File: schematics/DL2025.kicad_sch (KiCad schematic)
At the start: 8 parts, among them J1 Micro_SD_Card, U1 ATmega328PB-A, U2 DS18B20, U3 BMP280, U6 AMS1117-3.3, U7 AMS1117-3.3, U8 CC56-12GWA, U9 AMS1117-3.3

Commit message: Add files via upload
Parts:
- added U4: SC16IS750xPW, Package_SO:TSSOP-24_4.4x7.8mm_P0.65mm, symbol Interface_UART:SC16IS750xPW
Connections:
- net +5V: now also U4.7 (VDD)
- net GND: now also U3.1 (GND), U4.19 (VSS); no longer J1.5 (CLK), U1.17 (PB5)
- net at J1.3 (CMD), U1.16 (PB4): no longer J1.4 (VDD), U9.2 (VO)
- net at U1.30 (PD0): now also U4.2 (TX)
- net at U1.31 (PD1): now also U4.3 (RX)
- net at U3.2 (CSB): now also U3.6 (VDDIO), U3.8 (VDD), U6.2 (VO); no longer U3.1 (GND)
- net at U3.5 (SDO): no longer U3.6 (VDDIO)
- new net: J1.5 (CLK), U1.17 (PB5)
- new net: J1.4 (VDD), U9.2 (VO)
- no-connect marks 0 -> 34
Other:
- note added: "SDO POWINNO BYĆ PODŁĄCZONE DO GND LUB VCC ALE NIE DZIAŁA XD"
- moved on the sheet: U3

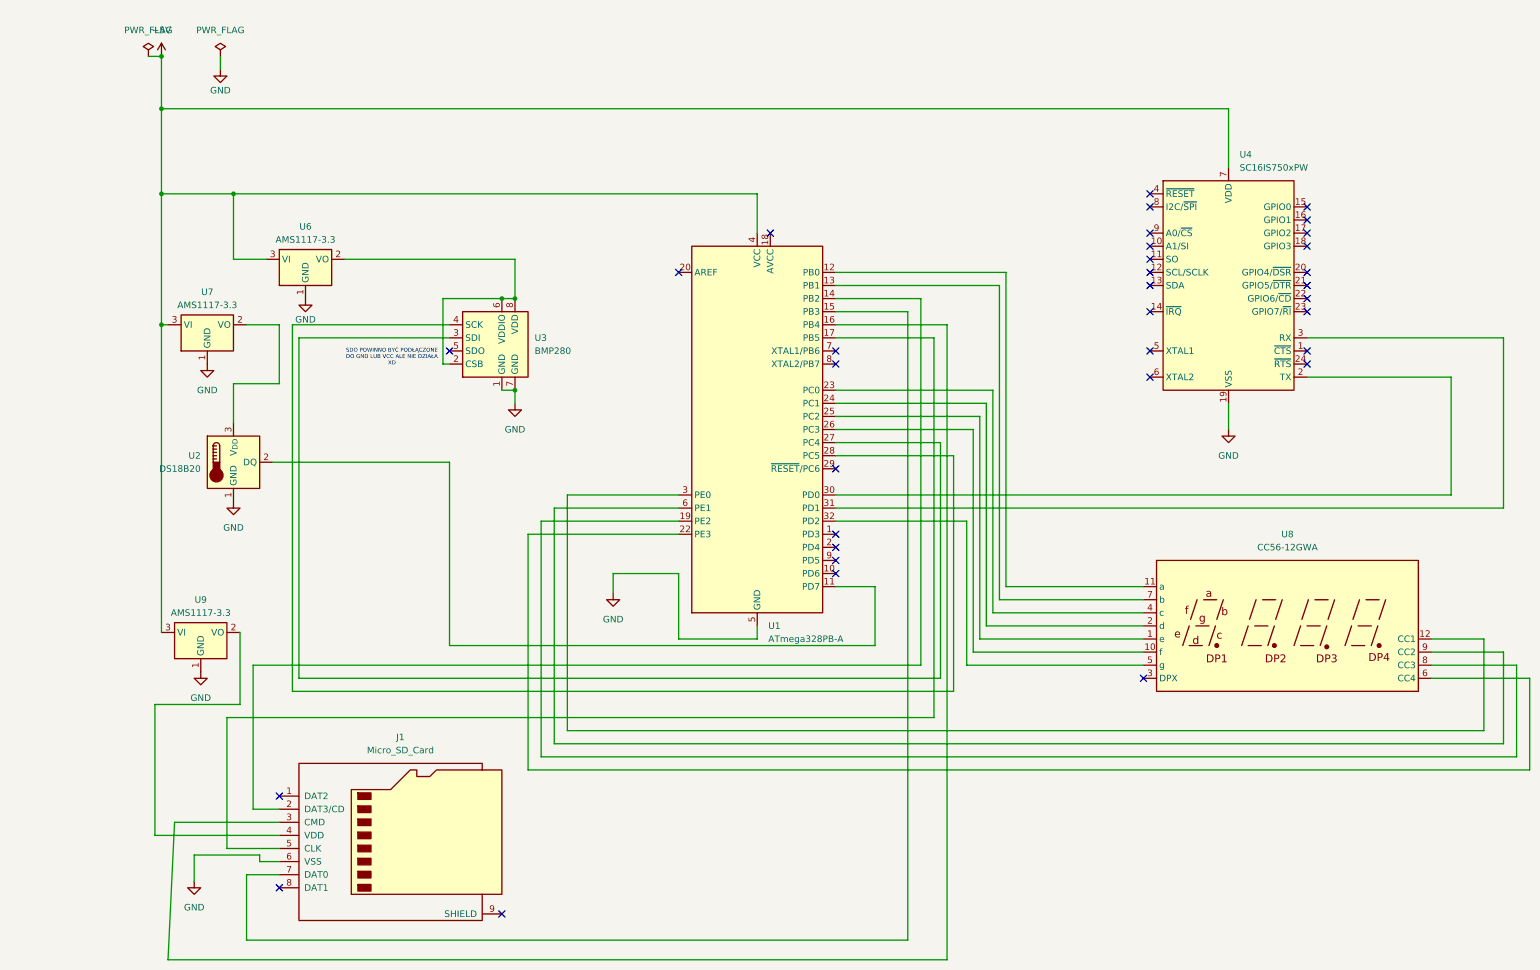
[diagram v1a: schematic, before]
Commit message: Updated schematics, just one AMS1117
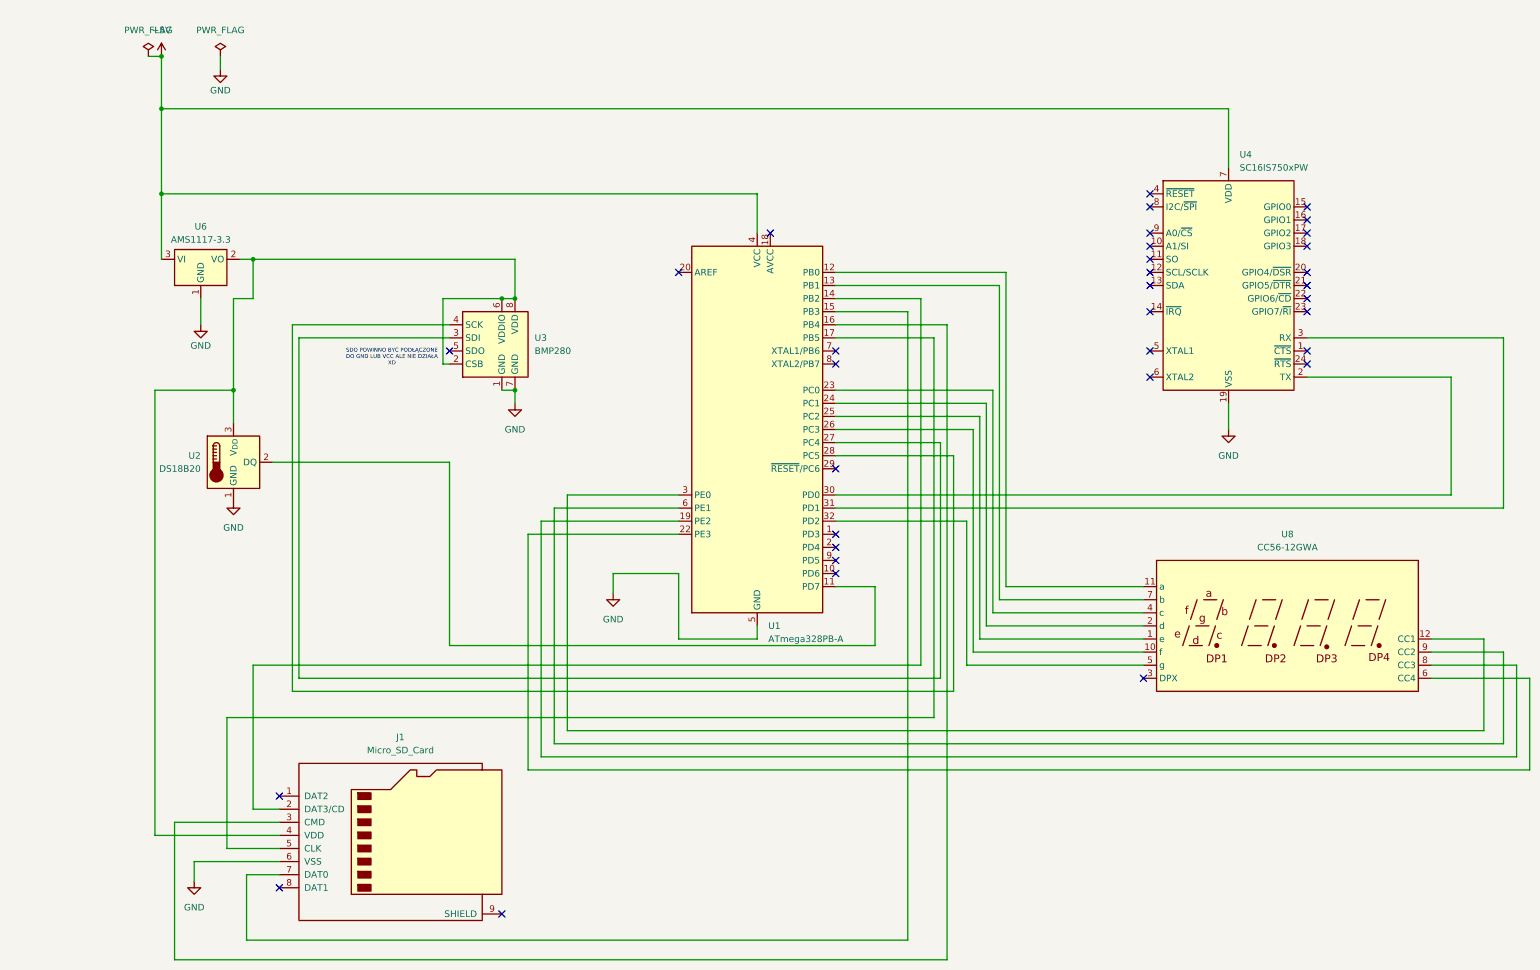
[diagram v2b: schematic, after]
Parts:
- removed U7, U9: AMS1117-3.3, Package_TO_SOT_SMD:SOT-223-3_TabPin2, symbol Regulator_Linear:AMS1117-3.3
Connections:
- net at J1.4 (VDD): now also U2.3 (V_{DD}), U3.2 (CSB), U3.6 (VDDIO), U3.8 (VDD), U6.2 (VO)
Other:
- moved on the sheet: U6

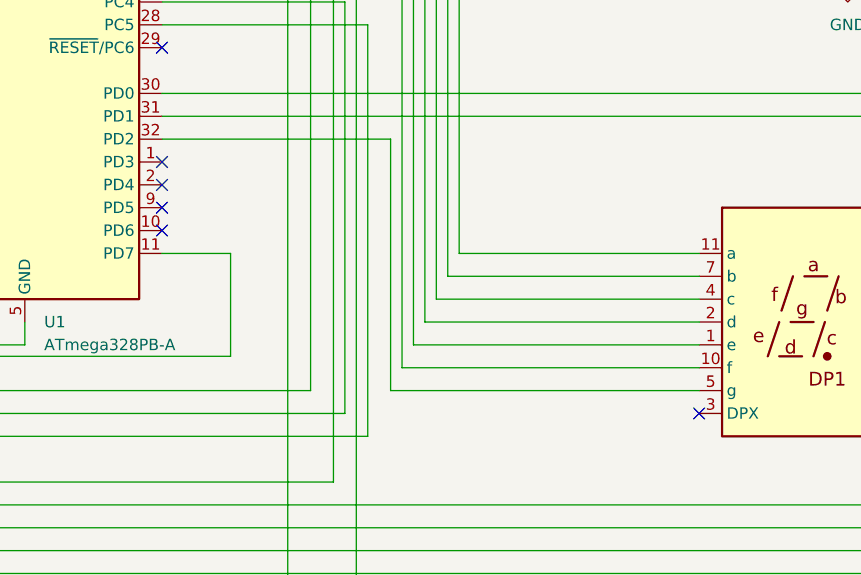
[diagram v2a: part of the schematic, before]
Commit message: Updated schematics, added LCD_DP -> PC3 connection
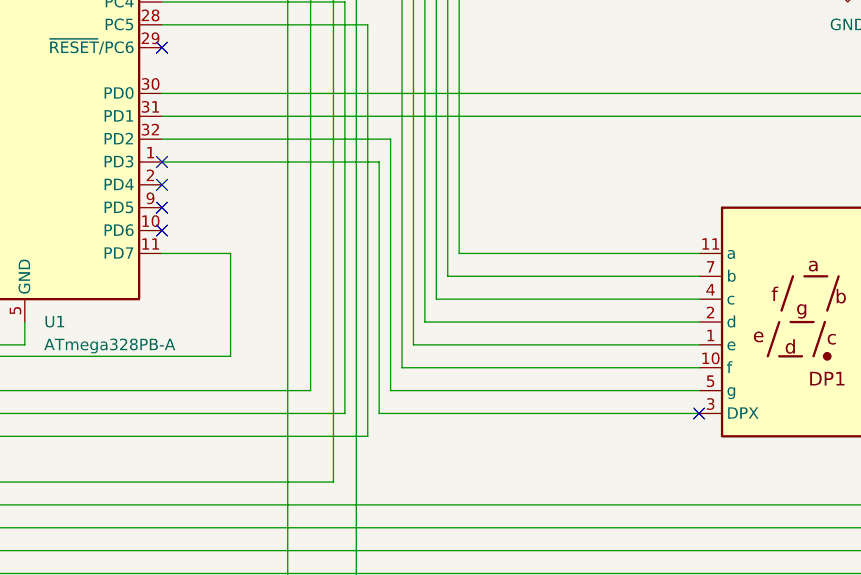
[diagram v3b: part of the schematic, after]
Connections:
- net at U1.1 (PD3): now also U8.3 (DPX)
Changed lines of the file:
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@@
+	(wire
+		(pts
+			(xy 148.59 111.76) (xy 172.72 111.76)
+		)
+		(stroke
+			(width 0)
+			(type default)
+		)
+	)
 	(wire
 		(pts
@@
 	(wire
 		(pts
+			(xy 172.72 139.7) (xy 208.28 139.7)
+		)
+		(stroke
+			(width 0)
+			(type default)
+		)
+	)
+	(wire
+		(pts
 			(xy 17.78 19.05) (xy 17.78 29.21)
 		)
@@
 		)
 		(stroke
+			(width 0)
+			(type default)
+		)
+	)
+	(wire
+		(pts
+			(xy 172.72 111.76) (xy 172.72 139.7)
+		)
+		(stroke

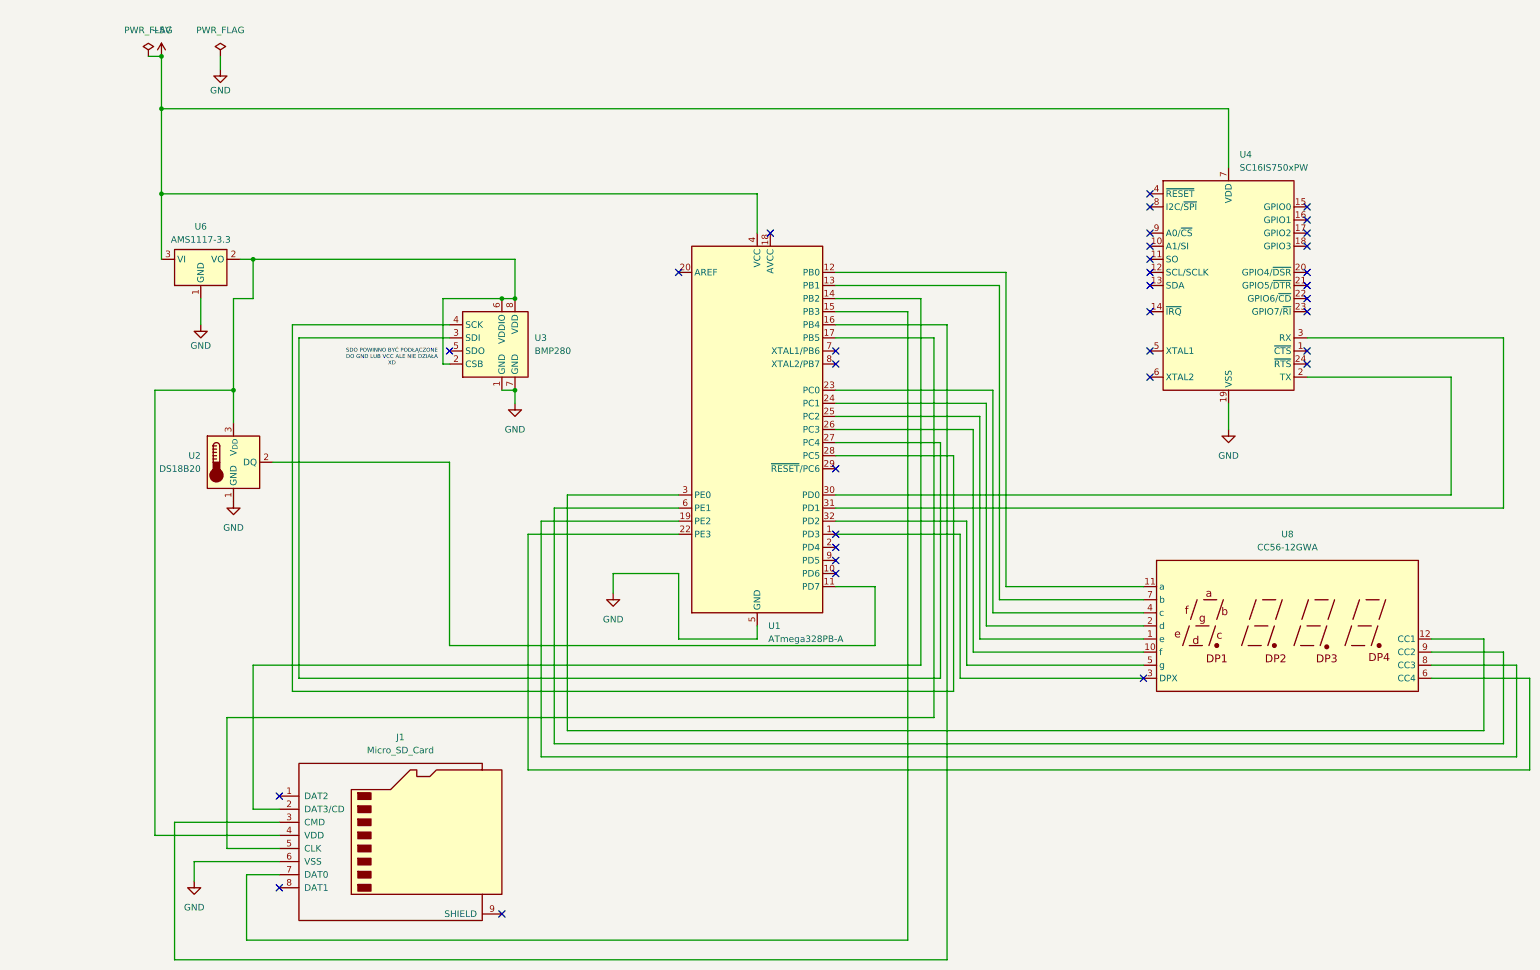
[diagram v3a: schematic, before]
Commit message: updated schematic, added capacitors
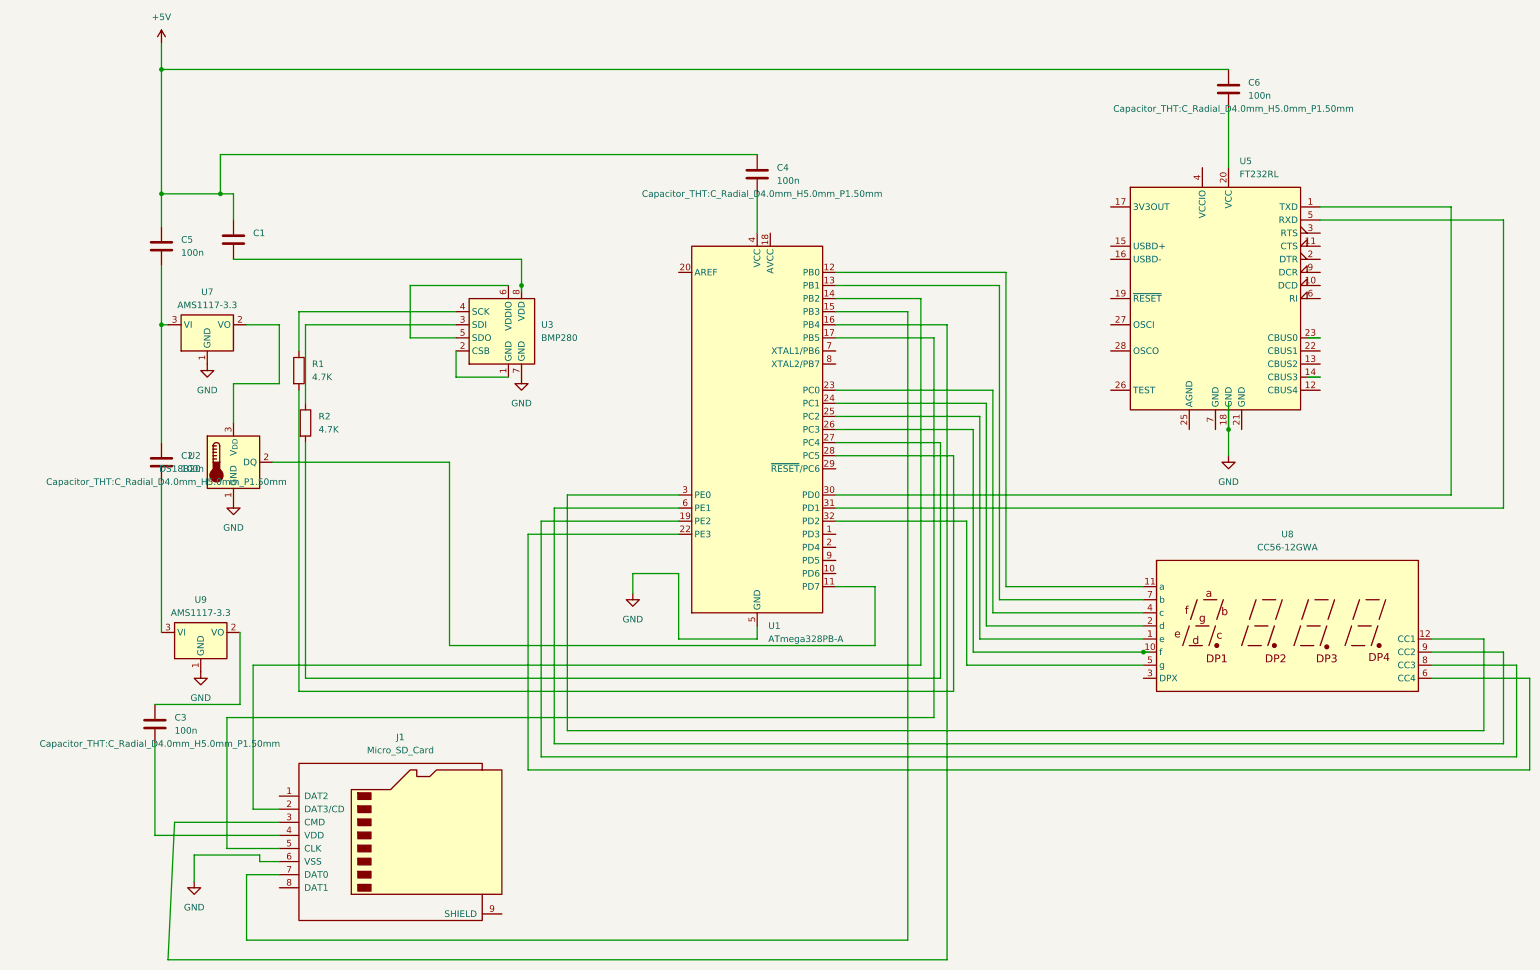
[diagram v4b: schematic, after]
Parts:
- removed U4: SC16IS750xPW, Package_SO:TSSOP-24_4.4x7.8mm_P0.65mm, symbol Interface_UART:SC16IS750xPW
- removed U6: AMS1117-3.3, Package_TO_SOT_SMD:SOT-223-3_TabPin2, symbol Regulator_Linear:AMS1117-3.3
- added C1, C2, C3, C4, C5, C6: 100n, Capacitor_THT:C_Radial_D4.0mm_H5.0mm_P1.50mm, symbol Device:C
- added R1, R2: 4.7K, Resistor_THT:R_Axial_DIN0207_L6.3mm_D2.5mm_P2.54mm_Vertical, symbol Device:R
- added U5: FT232RL, Package_SO:SSOP-28_5.3x10.2mm_P0.65mm, symbol Interface_USB:FT232RL
- added U7, U9: AMS1117-3.3, Package_TO_SOT_SMD:SOT-223-3_TabPin2, symbol Regulator_Linear:AMS1117-3.3
- J1: footprint (none) -> Connector_PinHeader_1.00mm:PinHeader_1x09_P1.00mm_Horizontal
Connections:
- net +5V: now also C1.1, C4.1, C5.1, C6.1; no longer U1.4 (VCC)
- net GND: now also U5.18 (GND), U7.1 (GND), U9.1 (GND); no longer U3.1 (GND)
- net at U1.1 (PD3): no longer U8.3 (DPX)
- net at U1.27 (PC4): now also R2.2; no longer U3.3 (SDI)
- net at U1.28 (PC5): now also R1.2; no longer U3.4 (SCK)
- net at U1.30 (PD0): now also U5.1 (TXD)
- net at U1.31 (PD1): now also U5.5 (RXD)
- net at U3.5 (SDO): now also U3.6 (VDDIO)
- new net: C3.1, U9.2 (VO)
- new net: C3.2, J1.4 (VDD)
- new net: C4.2, U1.4 (VCC)
- new net: C2.1, C5.2, U7.3 (VI)
- new net: C6.2, U5.20 (VCC)
- new net: C2.2, U9.3 (VI)
- new net: U3.1 (GND), U3.2 (CSB)
- new net: R2.1, U3.3 (SDI)
- new net: R1.1, U3.4 (SCK)
- new net: C1.2, U3.8 (VDD)
- new net: U2.3 (V_{DD}), U7.2 (VO)
- no-connect marks 34 -> 0
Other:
- note removed: "SDO POWINNO BYĆ PODŁĄCZONE DO GND LUB VCC ALE NIE DZIAŁA XD"
- moved on the sheet: U3

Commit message: updated schematics
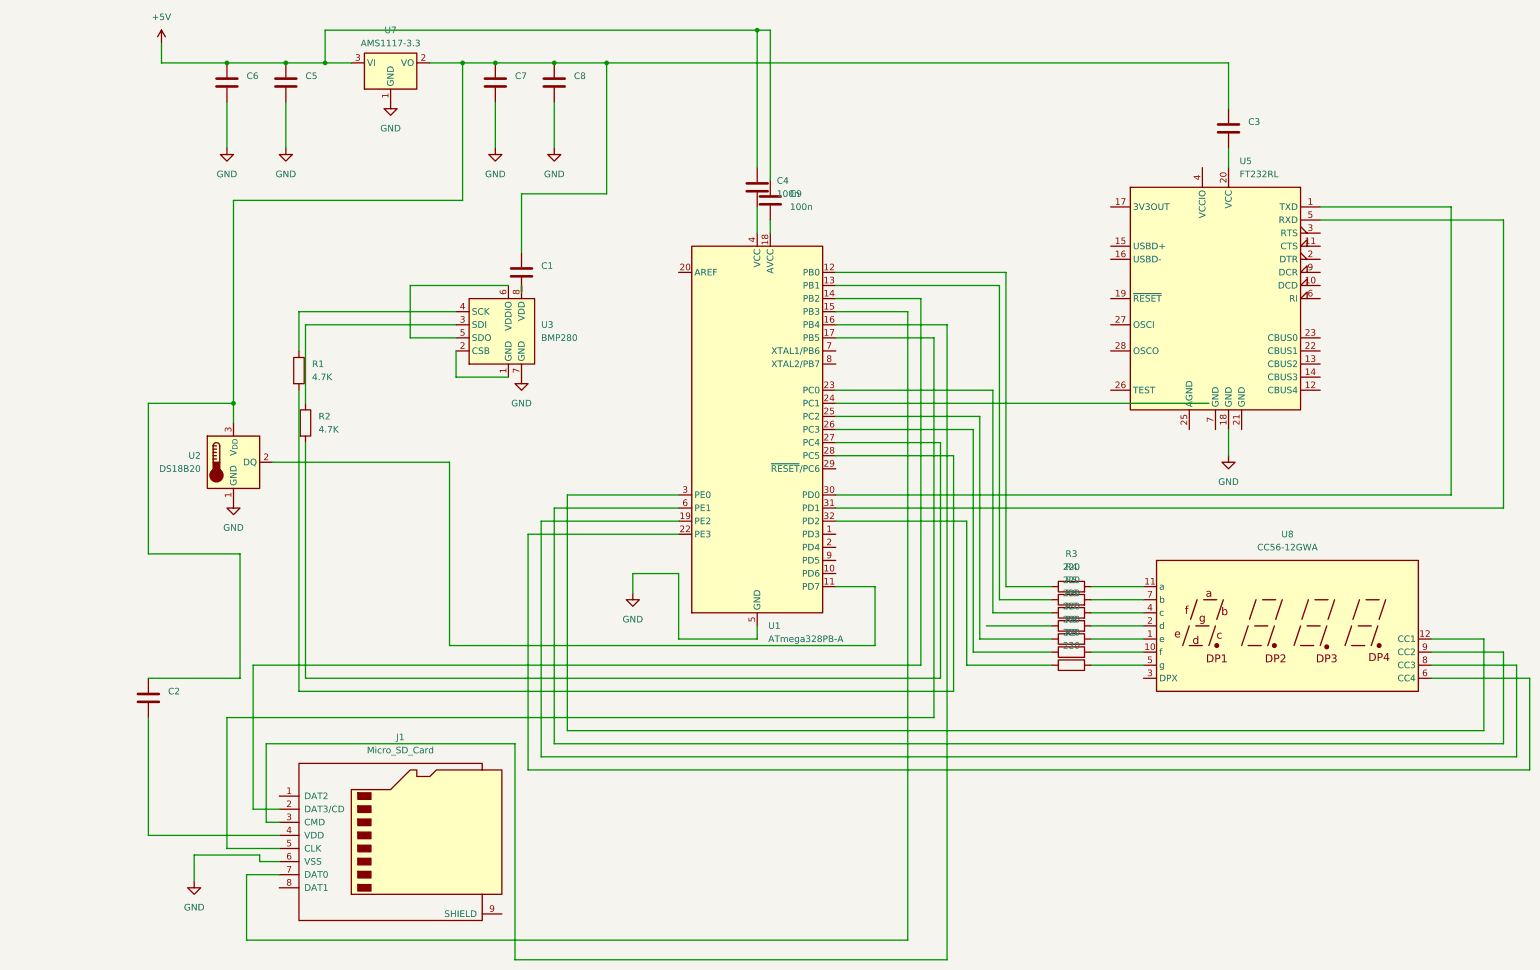
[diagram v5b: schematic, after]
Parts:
- removed U9: AMS1117-3.3, Package_TO_SOT_SMD:SOT-223-3_TabPin2, symbol Regulator_Linear:AMS1117-3.3
- added C7, C9: 100n, Capacitor_SMD:CP_Elec_4x3, symbol Device:C
- added C8: 10u, Capacitor_THT:CP_Radial_D4.0mm_P1.50mm, symbol Device:C
- added R3, R4, R5, R6, R7, R8, R9: 220, Resistor_SMD:R_0508_1220Metric_Pad1.12x2.15mm_HandSolder, symbol Device:R
- C1, C2, C3, C4, C5: footprint Capacitor_THT:C_Radial_D4.0mm_H5.0mm_P1.50mm -> Capacitor_SMD:CP_Elec_4x3
- C6: value 100n -> 10u; footprint Capacitor_THT:C_Radial_D4.0mm_H5.0mm_P1.50mm -> Capacitor_THT:CP_Radial_D4.0mm_P1.50mm
- R1, R2: footprint Resistor_THT:R_Axial_DIN0207_L6.3mm_D2.5mm_P2.54mm_Vertical -> Resistor_SMD:R_0508_1220Metric_Pad1.12x2.15mm_HandSolder
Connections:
- net +5V: now also U7.3 (VI), C9.1; no longer C1.1
- net GND: now also C5.2, C6.2, C7.2, C8.2
- net at C3.1: now also C1.1, C2.1, U2.3 (V_{DD}), U7.2 (VO), C7.1, C8.1
- net at C3.2: now also U5.20 (VCC); no longer J1.4 (VDD)
- net at U1.12 (PB0): now also R3.1; no longer U8.11 (a)
- net at U1.13 (PB1): now also R4.1; no longer U8.7 (b)
- net at U1.18 (AVCC): now also C9.2
- net at U1.23 (PC0): now also R5.1; no longer U8.4 (c)
- net at U1.24 (PC1): no longer U8.2 (d)
- net at U1.25 (PC2): now also R7.1; no longer U8.1 (e)
- net at U1.26 (PC3): now also R8.1; no longer U8.10 (f)
- net at U1.32 (PD2): now also R9.1; no longer U8.5 (g)
- net at C2.2: now also J1.4 (VDD)
- new net: R9.2, U8.5 (g)
- new net: R7.2, U8.1 (e)
- new net: R5.2, U8.4 (c)
- new net: R6.2, U8.2 (d)
- new net: R8.2, U8.10 (f)
- new net: R3.2, U8.11 (a)
- new net: R4.2, U8.7 (b)
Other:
- moved on the sheet: C1, C4, U7
